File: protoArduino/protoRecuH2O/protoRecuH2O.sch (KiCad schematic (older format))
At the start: 14 parts

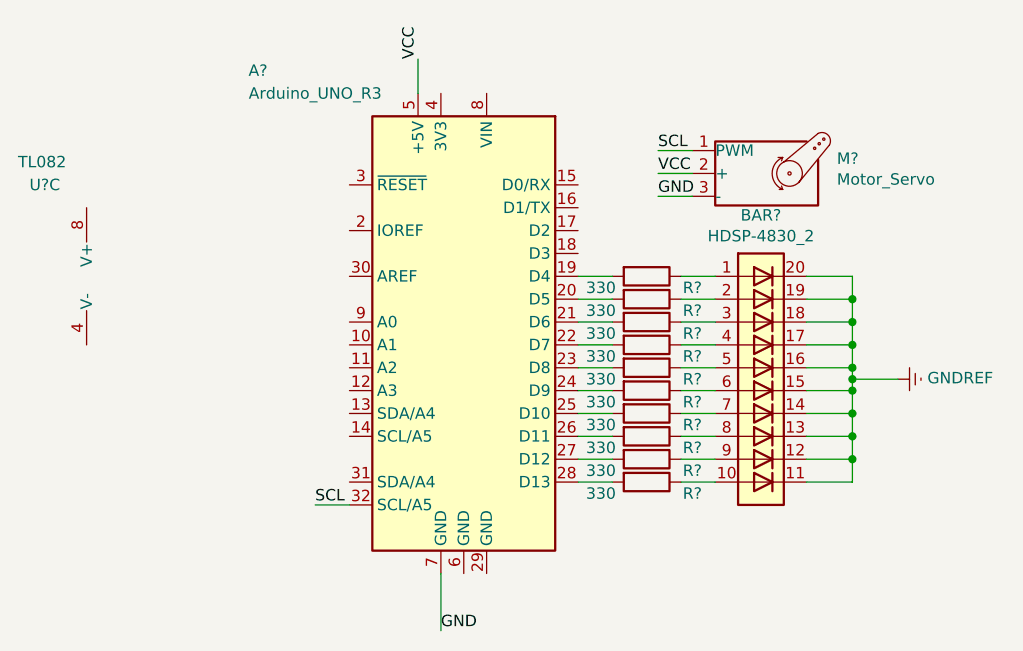
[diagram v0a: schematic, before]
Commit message: schéma électrique
j'ai fais le câblage de la sonde et j'ai modifier le câblage du moteur
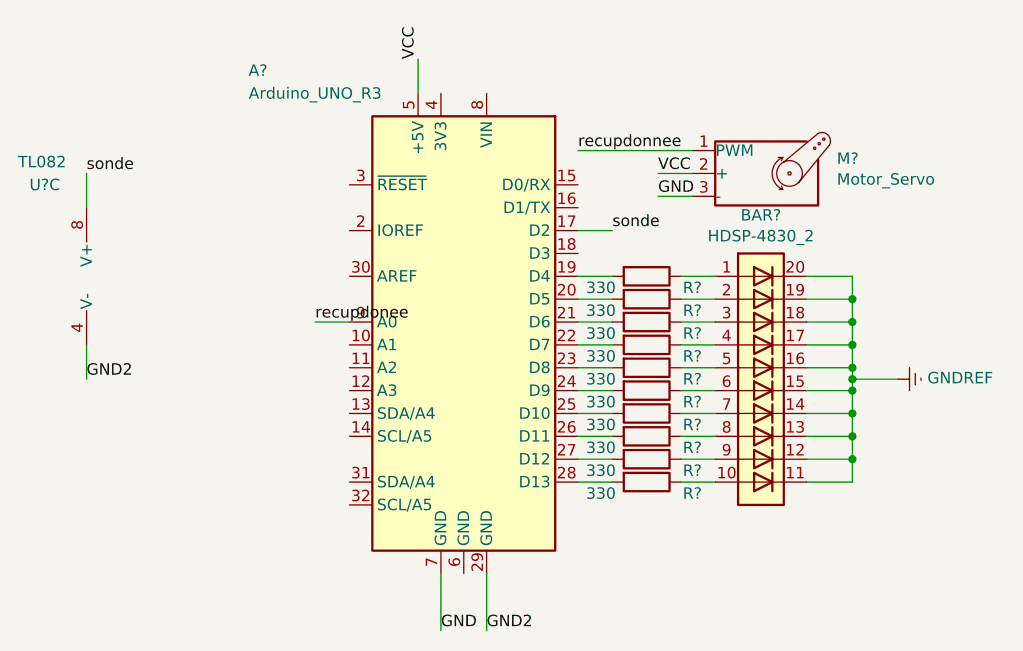
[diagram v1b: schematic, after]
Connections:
- net sonde: now reaches A?.17 (D2)
- net sonde: now also U?.8 (V+)
- net GND2: now reaches A?.29 (GND)
- net GND2: now also U?.4 (V-)
- net recupdonee: now reaches A?.9 (A0)
- net SCL: no longer names the net of A?.32 (SCL/A5)
- net SCL: no longer M?.1 (PWM)
- new net recupdonnee: M?.1 (PWM)
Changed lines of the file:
@@
 $EndComp
 Wire Wire Line
-	2550 4150 2400 4150
+	3150 4450 3150 4700
+Text Label 3150 4700 0    50   ~ 0
+GND2
 Wire Wire Line
-	4050 2600 3900 2600
-Text Label 2400 4150 0    50   ~ 0
-SCL
-Text Label 3900 2600 0    50   ~ 0
-SCL
+	1400 3450 1400 3600
+Text Label 1400 3600 0    50   ~ 0
+GND2
+Wire Wire Line
+	3550 2950 3700 2950
+Wire Wire Line
+	1400 2850 1400 2700
+Text Label 3700 2950 0    50   ~ 0
+sonde
+Text Label 1400 2700 0    50   ~ 0
+sonde
+Wire Wire Line
+	4050 2600 3550 2600
+Wire Wire Line
+	2550 3350 2400 3350
+Text Label 3550 2600 0    50   ~ 0
+recupdonnee
+Text Label 2400 3350 0    50   ~ 0
+recupdonee
 $EndSCHEMATC

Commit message: modifications
j'ai fais des modifications dans le schéma électrique, dans le code et dans le logigramme. J'ai aussi ajouté le lien du servo moteur dans la BOM
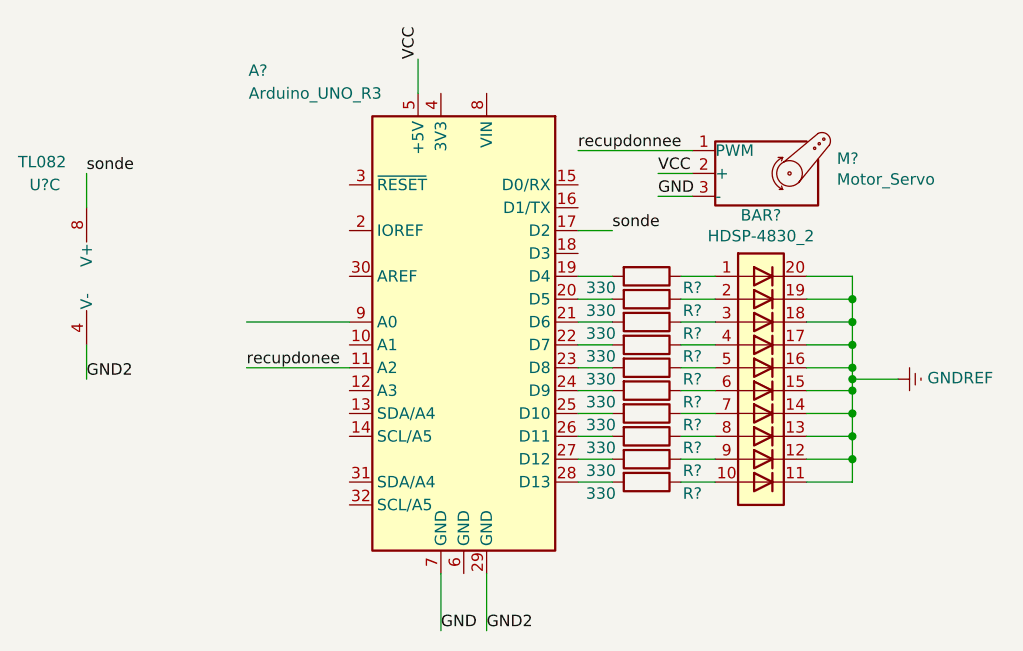
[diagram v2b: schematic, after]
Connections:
- net recupdonee: now also A?.11 (A2); no longer A?.9 (A0)
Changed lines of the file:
@@
 Wire Wire Line
 	4050 2600 3550 2600
-Wire Wire Line
-	2550 3350 2400 3350
 Text Label 3550 2600 0    50   ~ 0
 recupdonnee
-Text Label 2400 3350 0    50   ~ 0
+Text Label 2100 3550 0    50   ~ 0
 recupdonee
+Wire Wire Line
+	2550 3350 2100 3350
+Wire Wire Line
+	2550 3550 2100 3550
 $EndSCHEMATC

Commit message: mise a jour code, schéma eléctrique et logigramme
j'ai codé le moteur, j'ai modifier les noms des labels en fonction des noms donnés dans le code et j'ai modifier le logigramme
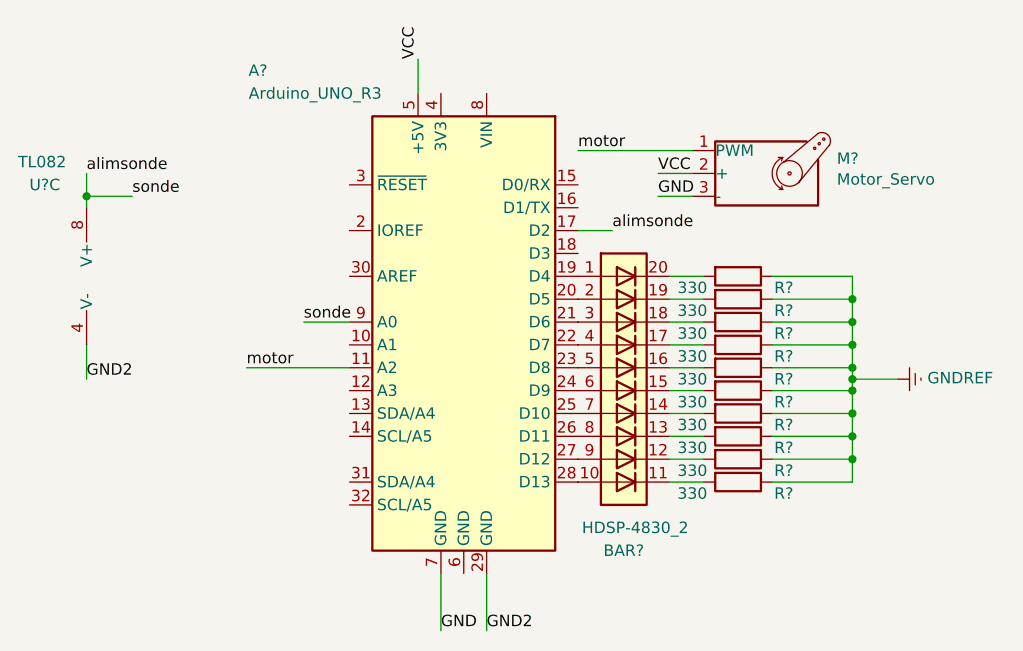
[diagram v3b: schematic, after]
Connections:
- net recupdonnee is gone; now on net motor: M?.1 (PWM)
- net sonde is gone; now on net alimsonde: A?.17 (D2), U?.8 (V+)
- net GNDREF: now also R?.1, R?.1, R?.1, R?.1, R?.1, R?.1, R?.1, R?.1, R?.1, R?.1; no longer BAR?.11 (K), BAR?.12 (K), BAR?.13 (K), BAR?.14 (K), BAR?.15 (K), BAR?.16 (K), BAR?.17 (K), BAR?.18 (K), BAR?.19 (K), BAR?.20 (K)
- net at BAR?.1 (A): now also A?.19 (D4); no longer R?.1
- net at BAR?.10 (A): now also A?.28 (D13); no longer R?.1
- net at BAR?.2 (A): now also A?.20 (D5); no longer R?.1
- net at BAR?.3 (A): now also A?.21 (D6); no longer R?.1
- net at BAR?.4 (A): now also A?.22 (D7); no longer R?.1
- net at BAR?.5 (A): now also A?.23 (D8); no longer R?.1
- net at BAR?.6 (A): now also A?.24 (D9); no longer R?.1
- net at BAR?.7 (A): now also A?.25 (D10); no longer R?.1
- net at BAR?.8 (A): now also A?.26 (D11); no longer R?.1
- net at BAR?.9 (A): now also A?.27 (D12); no longer R?.1
- net at R?.2: now also BAR?.20 (K); no longer A?.19 (D4)
- net at R?.2: now also BAR?.19 (K); no longer A?.20 (D5)
- net at R?.2: now also BAR?.18 (K); no longer A?.21 (D6)
- net at R?.2: now also BAR?.17 (K); no longer A?.22 (D7)
- net at R?.2: now also BAR?.16 (K); no longer A?.23 (D8)
- net at R?.2: now also BAR?.15 (K); no longer A?.24 (D9)
- net at R?.2: now also BAR?.14 (K); no longer A?.25 (D10)
- net at R?.2: now also BAR?.13 (K); no longer A?.26 (D11)
- net at R?.2: now also BAR?.12 (K); no longer A?.27 (D12)
- net at R?.2: now also BAR?.11 (K); no longer A?.28 (D13)
- net alimsonde: now reaches A?.9 (A0)
- net recupdonee renamed motor
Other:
- moved on the sheet: BAR?, R?
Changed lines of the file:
@@
 L LED:HDSP-4830_2 BAR?
 U 1 1 5EE0DBEF
-P 4350 3550
-F 0 "BAR?" H 4350 4217 50  0000 C CNN
-F 1 "HDSP-4830_2" H 4350 4126 50  0000 C CNN
-F 2 "Display:HDSP-4830" H 4350 2750 50  0001 C CNN
-F 3 "https://docs.broadcom.com/docs/AV02-1798EN" H 2350 3750 50  0001 C CNN
-	1    4350 3550
+P 3750 3550
+F 0 "BAR?" H 3750 2750 50  0000 C CNN
+F 1 "HDSP-4830_2" H 3800 2850 50  0000 C CNN
+F 2 "Display:HDSP-4830" H 3750 2750 50  0001 C CNN
+F 3 "https://docs.broadcom.com/docs/AV02-1798EN" H 1750 3750 50  0001 C CNN
+	1    3750 3550
 	1    0    0    -1
 $EndComp
@@
 L Device:R R?
 U 1 1 5EE1329C
-P 3850 4050
-F 0 "R?" V 3900 4250 50  0000 C CNN
-F 1 "330" V 3900 3850 50  0000 C CNN
-F 2 "" V 3780 4050 50  0001 C CNN
-F 3 "~" H 3850 4050 50  0001 C CNN
-	1    3850 4050
+P 4250 4050
+F 0 "R?" V 4300 4250 50  0000 C CNN
+F 1 "330" V 4300 3850 50  0000 C CNN
+F 2 "" V 4180 4050 50  0001 C CNN
+F 3 "~" H 4250 4050 50  0001 C CNN
+	1    4250 4050
 	0    1    1    0
 $EndComp
@@
 L Device:R R?
 U 1 1 5EE1456C
-P 3850 3950
-F 0 "R?" V 3900 4150 50  0000 C CNN
-F 1 "330" V 3900 3750 50  0000 C CNN
-F 2 "" V 3780 3950 50  0001 C CNN
-F 3 "~" H 3850 3950 50  0001 C CNN
-	1    3850 3950
+P 4250 3950
+F 0 "R?" V 4300 4150 50  0000 C CNN
+F 1 "330" V 4300 3750 50  0000 C CNN
+F 2 "" V 4180 3950 50  0001 C CNN
+F 3 "~" H 4250 3950 50  0001 C CNN
+	1    4250 3950
 	0    1    1    0
 $EndComp
@@
 L Device:R R?
 U 1 1 5EE147D1
-P 3850 3850
-F 0 "R?" V 3900 4050 50  0000 C CNN
-F 1 "330" V 3900 3650 50  0000 C CNN
-F 2 "" V 3780 3850 50  0001 C CNN
-F 3 "~" H 3850 3850 50  0001 C CNN
-	1    3850 3850
+P 4250 3850
+F 0 "R?" V 4300 4050 50  0000 C CNN
+F 1 "330" V 4300 3650 50  0000 C CNN
+F 2 "" V 4180 3850 50  0001 C CNN
+F 3 "~" H 4250 3850 50  0001 C CNN
+	1    4250 3850
 	0    1    1    0
 $EndComp
@@
 L Device:R R?
 U 1 1 5EE148DB
-P 3850 3750
-F 0 "R?" V 3900 3950 50  0000 C CNN
-F 1 "330" V 3900 3550 50  0000 C CNN
-F 2 "" V 3780 3750 50  0001 C CNN
-F 3 "~" H 3850 3750 50  0001 C CNN
-	1    3850 3750
+P 4250 3750
+F 0 "R?" V 4300 3950 50  0000 C CNN
+F 1 "330" V 4300 3550 50  0000 C CNN
+F 2 "" V 4180 3750 50  0001 C CNN
+F 3 "~" H 4250 3750 50  0001 C CNN
+	1    4250 3750
 	0    1    1    0
 $EndComp
@@
 L Device:R R?
 U 1 1 5EE14A29
-P 3850 3650
-F 0 "R?" V 3900 3850 50  0000 C CNN
-F 1 "330" V 3900 3450 50  0000 C CNN
-F 2 "" V 3780 3650 50  0001 C CNN
-F 3 "~" H 3850 3650 50  0001 C CNN
-	1    3850 3650
+P 4250 3650
+F 0 "R?" V 4300 3850 50  0000 C CNN
+F 1 "330" V 4300 3450 50  0000 C CNN
+F 2 "" V 4180 3650 50  0001 C CNN
+F 3 "~" H 4250 3650 50  0001 C CNN
+	1    4250 3650
 	0    1    1    0
 $EndComp
@@
 L Device:R R?
 U 1 1 5EE14C29
-P 3850 3550
-F 0 "R?" V 3900 3750 50  0000 C CNN
-F 1 "330" V 3900 3350 50  0000 C CNN
-F 2 "" V 3780 3550 50  0001 C CNN
-F 3 "~" H 3850 3550 50  0001 C CNN
-	1    3850 3550
+P 4250 3550
+F 0 "R?" V 4300 3750 50  0000 C CNN
+F 1 "330" V 4300 3350 50  0000 C CNN
+F 2 "" V 4180 3550 50  0001 C CNN
+F 3 "~" H 4250 3550 50  0001 C CNN
+	1    4250 3550
 	0    1    1    0
 $EndComp
@@
 L Device:R R?
 U 1 1 5EE14D78
-P 3850 3450
-F 0 "R?" V 3900 3650 50  0000 C CNN
-F 1 "330" V 3900 3250 50  0000 C CNN
-F 2 "" V 3780 3450 50  0001 C CNN
-F 3 "~" H 3850 3450 50  0001 C CNN
-	1    3850 3450
+P 4250 3450
+F 0 "R?" V 4300 3650 50  0000 C CNN
+F 1 "330" V 4300 3250 50  0000 C CNN
+F 2 "" V 4180 3450 50  0001 C CNN
+F 3 "~" H 4250 3450 50  0001 C CNN
+	1    4250 3450
 	0    1    1    0
 $EndComp
@@
 L Device:R R?
 U 1 1 5EE14F5B
-P 3850 3350
-F 0 "R?" V 3900 3550 50  0000 C CNN
-F 1 "330" V 3900 3150 50  0000 C CNN
-F 2 "" V 3780 3350 50  0001 C CNN
-F 3 "~" H 3850 3350 50  0001 C CNN
-	1    3850 3350
+P 4250 3350
+F 0 "R?" V 4300 3550 50  0000 C CNN
+F 1 "330" V 4300 3150 50  0000 C CNN
+F 2 "" V 4180 3350 50  0001 C CNN
+F 3 "~" H 4250 3350 50  0001 C CNN
+	1    4250 3350
 	0    1    1    0
 $EndComp
@@
 L Device:R R?
 U 1 1 5EE150FA
-P 3850 3250
-F 0 "R?" V 3900 3450 50  0000 C CNN
-F 1 "330" V 3900 3050 50  0000 C CNN
-F 2 "" V 3780 3250 50  0001 C CNN
-F 3 "~" H 3850 3250 50  0001 C CNN
-	1    3850 3250
+P 4250 3250
+F 0 "R?" V 4300 3450 50  0000 C CNN
+F 1 "330" V 4300 3050 50  0000 C CNN
+F 2 "" V 4180 3250 50  0001 C CNN
+F 3 "~" H 4250 3250 50  0001 C CNN
+	1    4250 3250
 	0    1    1    0
 $EndComp
@@
 L Device:R R?
 U 1 1 5EE15322
-P 3850 3150
-F 0 "R?" V 3900 3350 50  0000 C CNN
-F 1 "330" V 3900 2950 50  0000 C CNN
-F 2 "" V 3780 3150 50  0001 C CNN
-F 3 "~" H 3850 3150 50  0001 C CNN
-	1    3850 3150
-	0    1    1    0
-$EndComp
-Wire Wire Line
-	3550 3150 3700 3150
-Wire Wire Line
-	3550 3250 3700 3250
-Wire Wire Line
-	3550 3350 3700 3350
-Wire Wire Line
-	3550 3450 3700 3450
-Wire Wire Line
-	3550 3550 3700 3550
-Wire Wire Line
-	3550 3650 3700 3650
-Wire Wire Line
-	3550 3750 3700 3750
-Wire Wire Line
-	3550 3850 3700 3850
-Wire Wire Line
-	3550 3950 3700 3950
-Wire Wire Line
-	3550 4050 3700 4050
-Wire Wire Line
-	4000 3150 4150 3150
-Wire Wire Line
-	4000 3250 4150 3250
-Wire Wire Line
-	4000 3350 4150 3350
-Wire Wire Line
-	4000 3450 4150 3450
-Wire Wire Line
-	4000 3550 4150 3550
-Wire Wire Line
-	4000 3650 4150 3650
-Wire Wire Line
-	4000 3750 4150 3750
-Wire Wire Line
-	4000 3850 4150 3850
-Wire Wire Line
-	4000 3950 4150 3950
-Wire Wire Line
-	4000 4050 4150 4050
-Wire Wire Line
-	4550 3150 4750 3150
+P 4250 3150
+F 0 "R?" V 4300 3350 50  0000 C CNN
+F 1 "330" V 4300 2950 50  0000 C CNN
+F 2 "" V 4180 3150 50  0001 C CNN
+F 3 "~" H 4250 3150 50  0001 C CNN
+	1    4250 3150
+	0    1    1    0
+$EndComp
+Wire Wire Line
+	3950 3150 4100 3150
+Wire Wire Line
+	3950 3250 4100 3250
+Wire Wire Line
+	3950 3350 4100 3350
+Wire Wire Line
+	3950 3450 4100 3450
+Wire Wire Line
+	3950 3550 4100 3550
+Wire Wire Line
+	3950 3650 4100 3650
+Wire Wire Line
+	3950 3750 4100 3750
+Wire Wire Line
+	3950 3850 4100 3850
+Wire Wire Line
+	3950 3950 4100 3950
+Wire Wire Line
+	3950 4050 4100 4050
 Wire Wire Line
 	4750 3150 4750 3250
-Wire Wire Line
-	4750 4050 4550 4050
 Wire Wire Line
 	4750 3600 4950 3600
@@
 	0    -1   -1   0
 $EndComp
-Wire Wire Line
-	4550 3250 4750 3250
 Connection ~ 4750 3250
 Wire Wire Line
 	4750 3250 4750 3350
-Wire Wire Line
-	4550 3350 4750 3350
 Connection ~ 4750 3350
 Wire Wire Line
 	4750 3350 4750 3450
-Wire Wire Line
-	4550 3450 4750 3450
 Connection ~ 4750 3450
 Wire Wire Line
 	4750 3450 4750 3550
-Wire Wire Line
-	4550 3550 4750 3550
 Connection ~ 4750 3550
 Wire Wire Line
 	4750 3550 4750 3600
-Wire Wire Line
-	4550 3650 4750 3650
 Connection ~ 4750 3650
 Wire Wire Line
 	4750 3650 4750 3750
-Wire Wire Line
-	4550 3750 4750 3750
 Connection ~ 4750 3750
 Wire Wire Line
 	4750 3750 4750 3850
-Wire Wire Line
-	4550 3850 4750 3850
 Connection ~ 4750 3850
 Wire Wire Line
 	4750 3850 4750 3950
-Wire Wire Line
-	4550 3950 4750 3950
 Connection ~ 4750 3950
 Wire Wire Line
@@
 	3550 2950 3700 2950
 Wire Wire Line
-	1400 2850 1400 2700
+	1400 2850 1400 2800
 Text Label 3700 2950 0    50   ~ 0
-sonde
+alimsonde
 Text Label 1400 2700 0    50   ~ 0
-sonde
+alimsonde
 Wire Wire Line
 	4050 2600 3550 2600
 Text Label 3550 2600 0    50   ~ 0
-recupdonnee
+motor
 Text Label 2100 3550 0    50   ~ 0
-recupdonee
-Wire Wire Line
-	2550 3350 2100 3350
+motor
 Wire Wire Line
 	2550 3550 2100 3550
+Wire Wire Line
+	4400 3150 4750 3150
+Wire Wire Line
+	4400 3250 4750 3250
+Wire Wire Line
+	4400 3350 4750 3350
+Wire Wire Line
+	4400 3450 4750 3450
+Wire Wire Line
+	4400 3550 4750 3550
+Wire Wire Line
+	4400 3650 4750 3650
+Wire Wire Line
+	4400 3750 4750 3750
+Wire Wire Line
+	4400 3850 4750 3850
+Wire Wire Line
+	4400 3950 4750 3950
+Wire Wire Line
+	4400 4050 4750 4050
+Wire Wire Line
+	1400 2800 1600 2800
+Connection ~ 1400 2800
+Wire Wire Line
+	1400 2800 1400 2700
+Wire Wire Line
+	2550 3350 2350 3350
+Text Label 1600 2800 0    50   ~ 0
+sonde
+Text Label 2350 3350 0    50   ~ 0
+sonde
 $EndSCHEMATC

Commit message: reset arduino code
Signed-off-by: darthjuda <mehdi.jung@me.com>
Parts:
- removed A?: Arduino_UNO_R3, Module:Arduino_UNO_R3, symbol MCU_Module:Arduino_UNO_R3
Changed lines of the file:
@@
 $EndDescr
-$Comp
-L MCU_Module:Arduino_UNO_R3 A?
-U 1 1 5EE0F7ED
-P 3050 3350
-F 0 "A?" H 3950 4450 50  0000 C CNN
-F 1 "Arduino_UNO_R3" H 3700 4350 50  0000 C CNN
-F 2 "Module:Arduino_UNO_R3" H 3050 3350 50  0001 C CIN
-F 3 "https://www.arduino.cc/en/Main/arduinoBoardUno" H 3050 3350 50  0001 C CNN
-	1    3050 3350
-	-1   0    0    -1
-$EndComp
 $Comp
 L LED:HDSP-4830_2 BAR?
